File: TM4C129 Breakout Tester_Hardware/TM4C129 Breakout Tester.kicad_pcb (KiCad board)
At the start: 2 copper layers, 134.6 x 101.6 mm, 157 parts, among them SW1 SW_Push, SW10 SW_Push, SW11 SW_Push, SW12 SW_Push, SW13 SW_Push, SW14 SW_Push, SW15 SW_Push, SW16 SW_Push, SW17 SW_Push, SW18 SW_Push, SW19 SW_Push, SW2 SW_Push, SW20 SW_Push, SW21 SW_Push, SW22 SW_Push, SW23 SW_Push, SW24 SW_Push, SW25 SW_Push, SW26 SW_Push, SW27 SW_Push, SW28 SW_Push, SW29 SW_Push, SW3 SW_Push, SW30 SW_Push, SW31 SW_Push, SW32 SW_Push, SW33 SW_Push, SW34 SW_Push, SW35 SW_Push, SW36 SW_Push, SW37 SW_Push, SW38 SW_Push, SW39 SW_Push, SW4 SW_Push, SW40 SW_Push, SW41 SW_Push, SW42 SW_Push, SW43 SW_Push, SW44 SW_Push, SW45 SW_Push, SW46 SW_Push, SW47 SW_Push, SW48 SW_Push, SW49 SW_Push, SW5 SW_Push, SW50 SW_DIP_x08, SW51 SW_DIP_x08, SW52 SW_DIP_x08, SW6 SW_Push, SW7 SW_Push, SW8 SW_Push, SW9 SW_Push, U1 OKI_3V3, U2 TM4C129Breakout

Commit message: Touchpus and Silkscreen
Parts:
- added D50: LED_Small, LED_SMD:LED_0603_1608Metric_Pad1.05x0.95mm_HandSolder, F.Cu at (155.8, 68.6)
- added G***: LOGO, MRDT_Silkscreens:z_sig_Andrew_Van_Horn_Sig_15mm, B.Cu at (142.7, 66.5)
- added G***: LOGO, MRDT_Silkscreens:0_MRDT_Logo_30mm, F.Cu at (115.8, 98.6)
- added R50: 500, Resistor_SMD:R_0603_1608Metric_Pad1.05x0.95mm_HandSolder, F.Cu at (152.0, 68.6)
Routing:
- net +3V3: track 745.2 -> 751.7 mm
- net Net-(D50-Pad2): track 0.00 -> 2.03 mm
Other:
- board text added: "+"
- board text added: "-"
- board text added: "Pot Bridge"
- board text added: "Power"
- board text added: "TM4C129 Breakout Tester, Rev 1 Mars Rover Design Team Missouri S&T, 2020 Andrew Van Horn"
- board text added: "Tx/Rx Bridge"

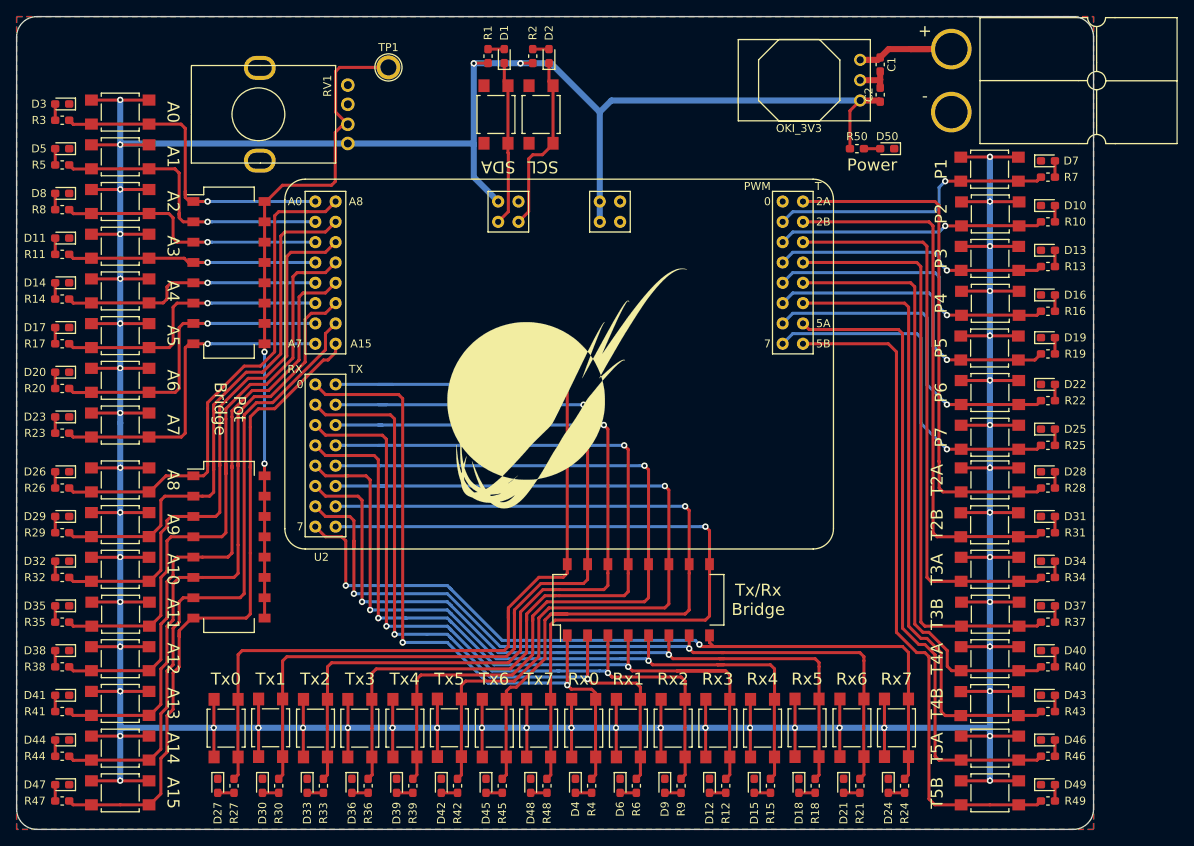
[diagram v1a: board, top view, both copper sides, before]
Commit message: Updated breakout footprint
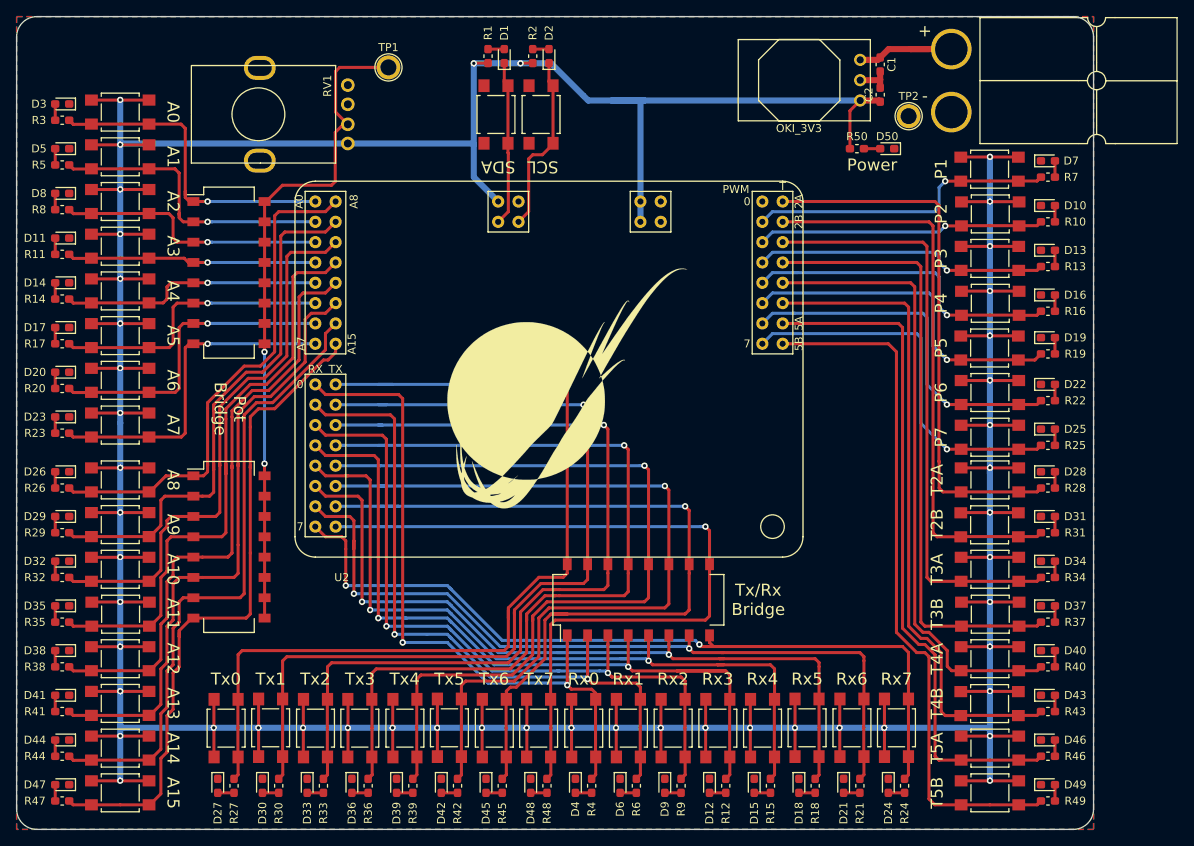
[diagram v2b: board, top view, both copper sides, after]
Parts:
- added TP2: TestPoint, TestPoint:TestPoint_Plated_Hole_D2.0mm, F.Cu at (158.5, 64.5)
- moved U2 3.59 mm to (84.3, 75.2)
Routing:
- net +3V3: track 751.7 -> 756.1 mm
- net PWM4: track 37.6 -> 40.6 mm
- net T5A: track 81.6 -> 84.6 mm
- net PWM6: track 42.8 -> 45.6 mm
- net T5B: track 84.8 -> 87.3 mm
- net T4B: track 78.9 -> 81.5 mm
- net T4A: track 75.9 -> 78.4 mm
- net T3B: track 74.9 -> 77.4 mm
- net T3A: track 71.8 -> 74.3 mm
- net T2B: track 68.7 -> 71.2 mm
- net T2A: track 65.7 -> 68.2 mm
- net PWM7: track 45.4 -> 48.0 mm
- net PWM5: track 40.4 -> 42.9 mm
- net PWM3: track 34.6 -> 37.1 mm
- net PWM2: track 33.3 -> 35.8 mm
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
